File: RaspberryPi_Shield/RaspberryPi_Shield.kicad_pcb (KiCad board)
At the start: 2 copper layers, 85.6 x 56.5 mm, 0 parts

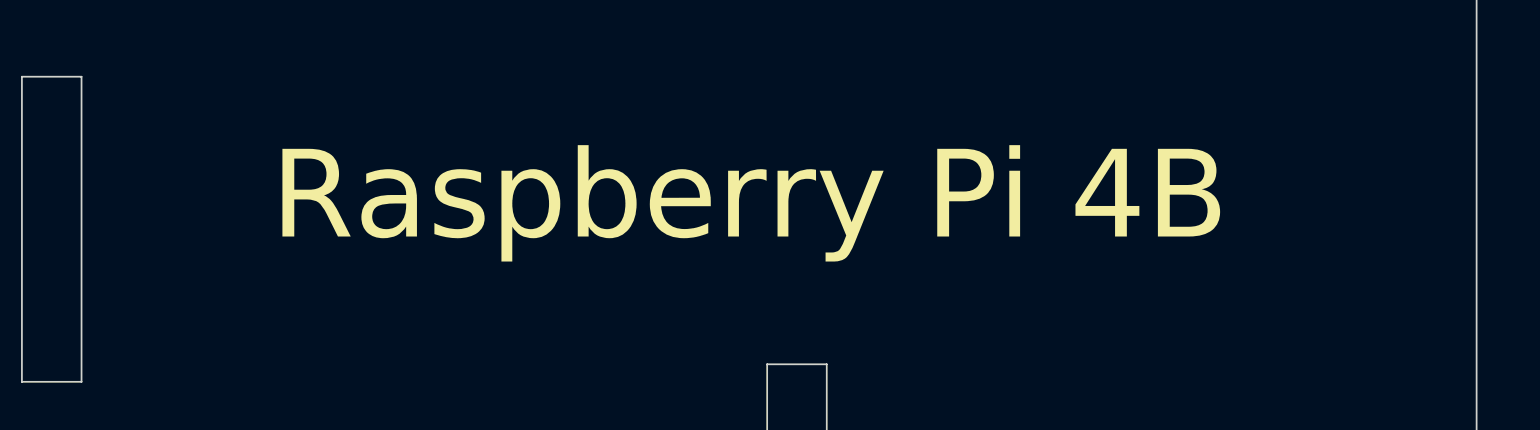
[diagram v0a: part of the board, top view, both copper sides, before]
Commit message: attach Raspberry logo
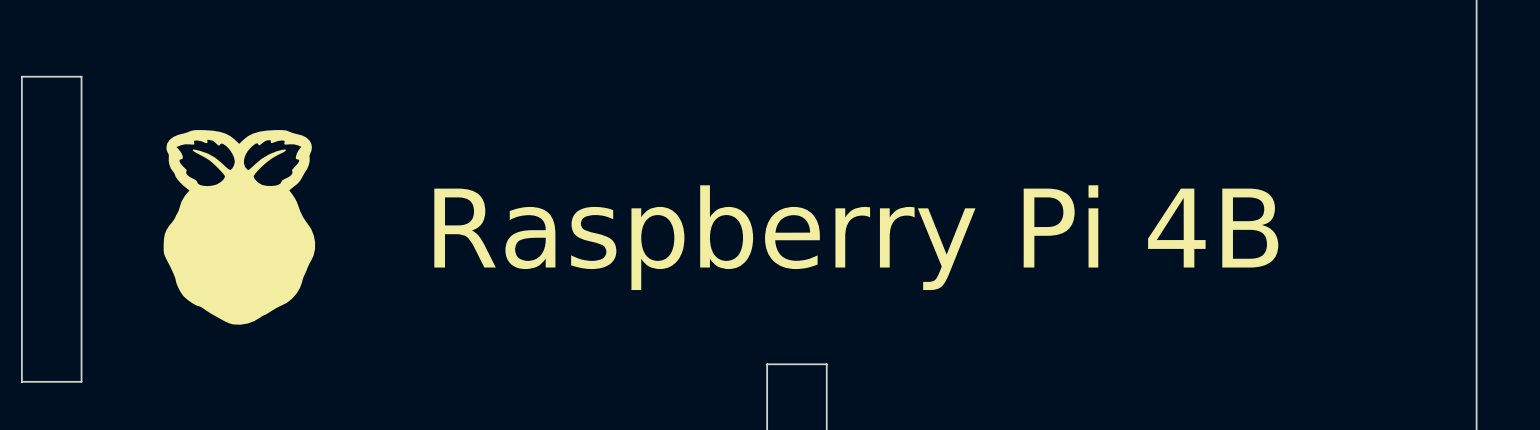
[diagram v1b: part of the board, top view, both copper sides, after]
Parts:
- added G***: LOGO, RaspberryLibrary:logo, F.Cu at (110.0, 97.0)

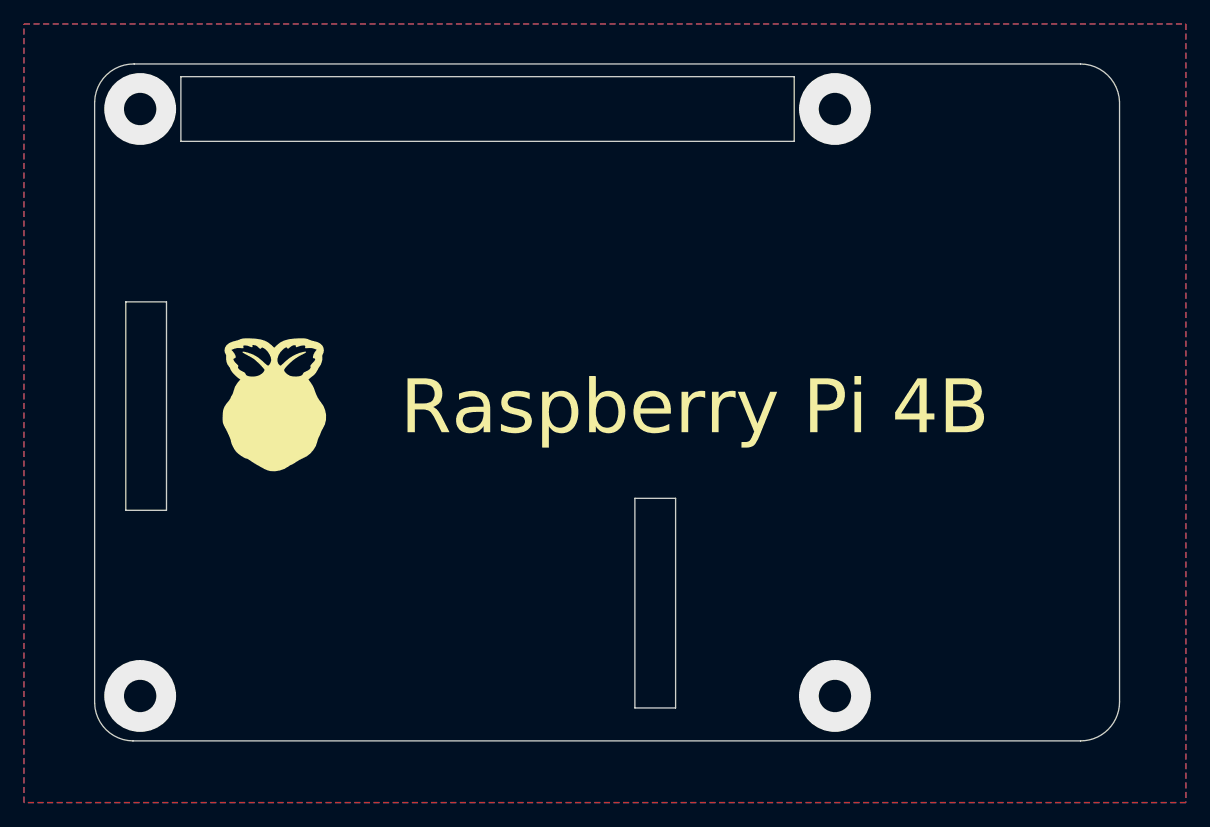
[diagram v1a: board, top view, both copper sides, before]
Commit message: expand board margin
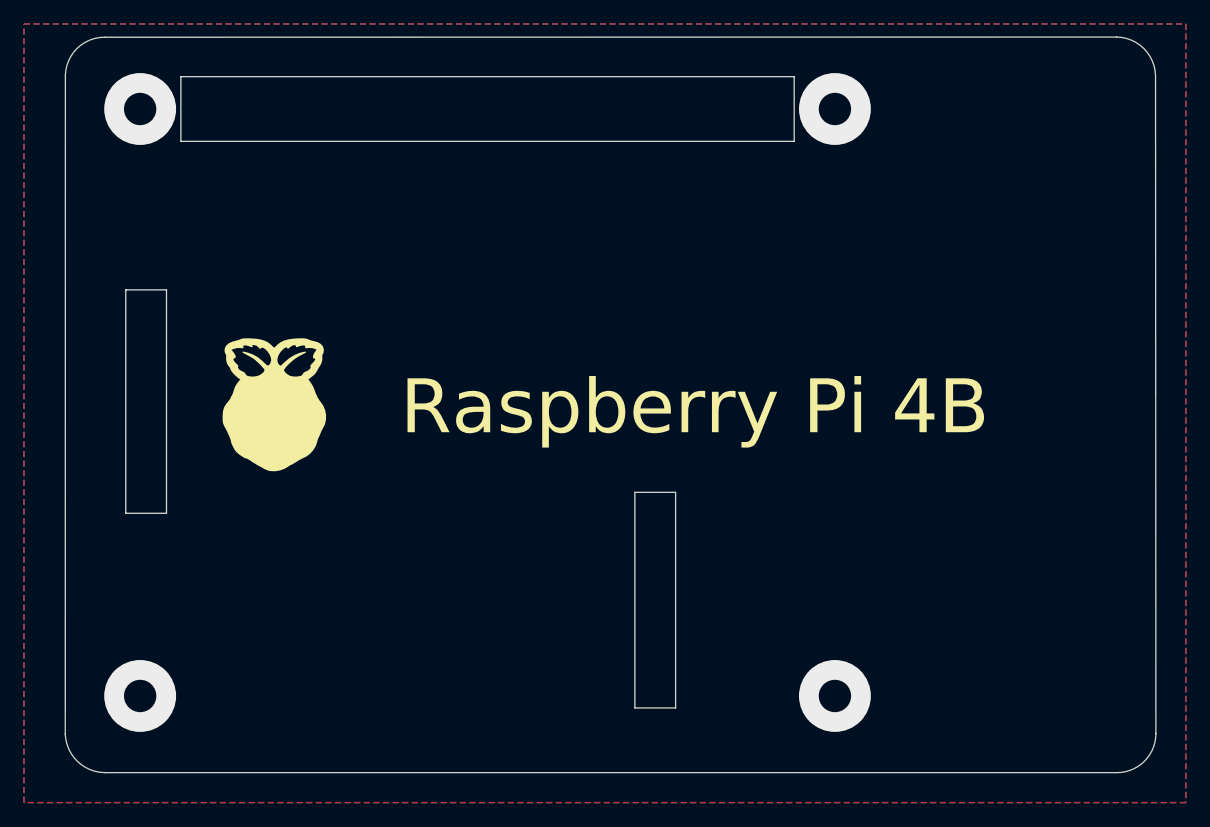
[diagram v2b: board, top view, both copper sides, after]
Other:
- board size 85.6 x 56.5 mm -> 91 x 61.4 mm
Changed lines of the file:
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@@
   (gr_line (start 131.15 85.525) (end 130.875 85.525) (layer "Dwgs.User") (width 0.2))
   (gr_line (start 107.355 95.1724) (end 107.3662 95.2535) (layer "Dwgs.User") (width 0.2))
-  (gr_arc (start 98.1 124.85) (mid 95.862424 123.922696) (end 94.9 121.7) (layer "Edge.Cuts") (width 0.1))
-  (gr_rect (start 140 104.6) (end 143.4 122.1) (layer "Edge.Cuts") (width 0.1) (fill none))
-  (gr_line (start 180.46 71.5) (end 180.46 121.6) (layer "Edge.Cuts") (width 0.1))
-  (gr_line (start 177.2 124.85) (end 98.1 124.85) (layer "Edge.Cuts") (width 0.1))
-  (gr_arc (start 180.46 121.6) (mid 179.504614 123.901213) (end 177.2 124.85) (layer "Edge.Cuts") (width 0.1))
-  (gr_rect (start 97.5 88.2) (end 100.9 105.6) (layer "Edge.Cuts") (width 0.1) (fill none))
+  (gr_arc (start 95.737576 127.5) (mid 93.458047 126.553139) (end 92.45 124.3) (layer "Edge.Cuts") (width 0.1))
+  (gr_rect (start 140 104.1) (end 143.4 122.1) (layer "Edge.Cuts") (width 0.1) (fill none))
+  (gr_line (start 183.464991 69.33937) (end 183.495617 124.248546) (layer "Edge.Cuts") (width 0.1))
+  (gr_line (start 180.24 127.5) (end 95.737576 127.5) (layer "Edge.Cuts") (width 0.1))
+  (gr_arc (start 183.495617 124.248546) (mid 182.541638 126.548965) (end 180.24 127.5) (layer "Edge.Cuts") (width 0.1))
+  (gr_rect (start 97.5 87.2) (end 100.9 105.85) (layer "Edge.Cuts") (width 0.1) (fill none))
   (gr_rect (start 102.1 69.4) (end 153.3 74.8) (layer "Edge.Cuts") (width 0.1) (fill none))
-  (gr_arc (start 177.2 68.34) (mid 179.463352 69.266605) (end 180.46 71.5) (layer "Edge.Cuts") (width 0.1))
-  (gr_arc (start 94.9 71.5) (mid 95.901086 69.242336) (end 98.2 68.34) (layer "Edge.Cuts") (width 0.1))
-  (gr_line (start 94.9 121.7) (end 94.9 71.5) (layer "Edge.Cuts") (width 0.1))
-  (gr_line (start 98.2 68.34) (end 177.2 68.34) (layer "Edge.Cuts") (width 0.1))
-  (gr_text "UinIO.com by Hank" (at 140 96) (layer "B.SilkS")
+  (gr_arc (start 180.208867 66.091698) (mid 182.495301 67.055448) (end 183.464991 69.33937) (layer "Edge.Cuts") (width 0.1))
+  (gr_arc (start 92.459029 69.283805) (mid 93.463406 67.016388) (end 95.771133 66.108303) (layer "Edge.Cuts") (width 0.1))
+  (gr_line (start 92.45 124.3) (end 92.459029 69.283805) (layer "Edge.Cuts") (width 0.1))
+  (gr_line (start 95.771133 66.108303) (end 180.208867 66.091698) (layer "Edge.Cuts") (width 0.1))
+  (gr_text "UinIO.com by Hank" (at 140 96) (layer "B.Paste")
     (effects (font (size 4 4) (thickness 0.8)) (justify mirror))
   )
